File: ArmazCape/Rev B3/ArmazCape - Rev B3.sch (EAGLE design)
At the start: 166 parts, among them M1 7490100111A, Q1 32.768kHz, 12.5pF, Q2 ASE, Q4 IRLML6344TRPBF, Q5 IRLML6344TRPBF, U1 L7985A, U2 L7985A, U3 DS1307ZN+, U4 24AA256-I/SN, U5 CD4050BD, U6 CD4050BD, U7 PCA9685PW, U8 SN65HVD08D, U9 KSZ8851SNLI

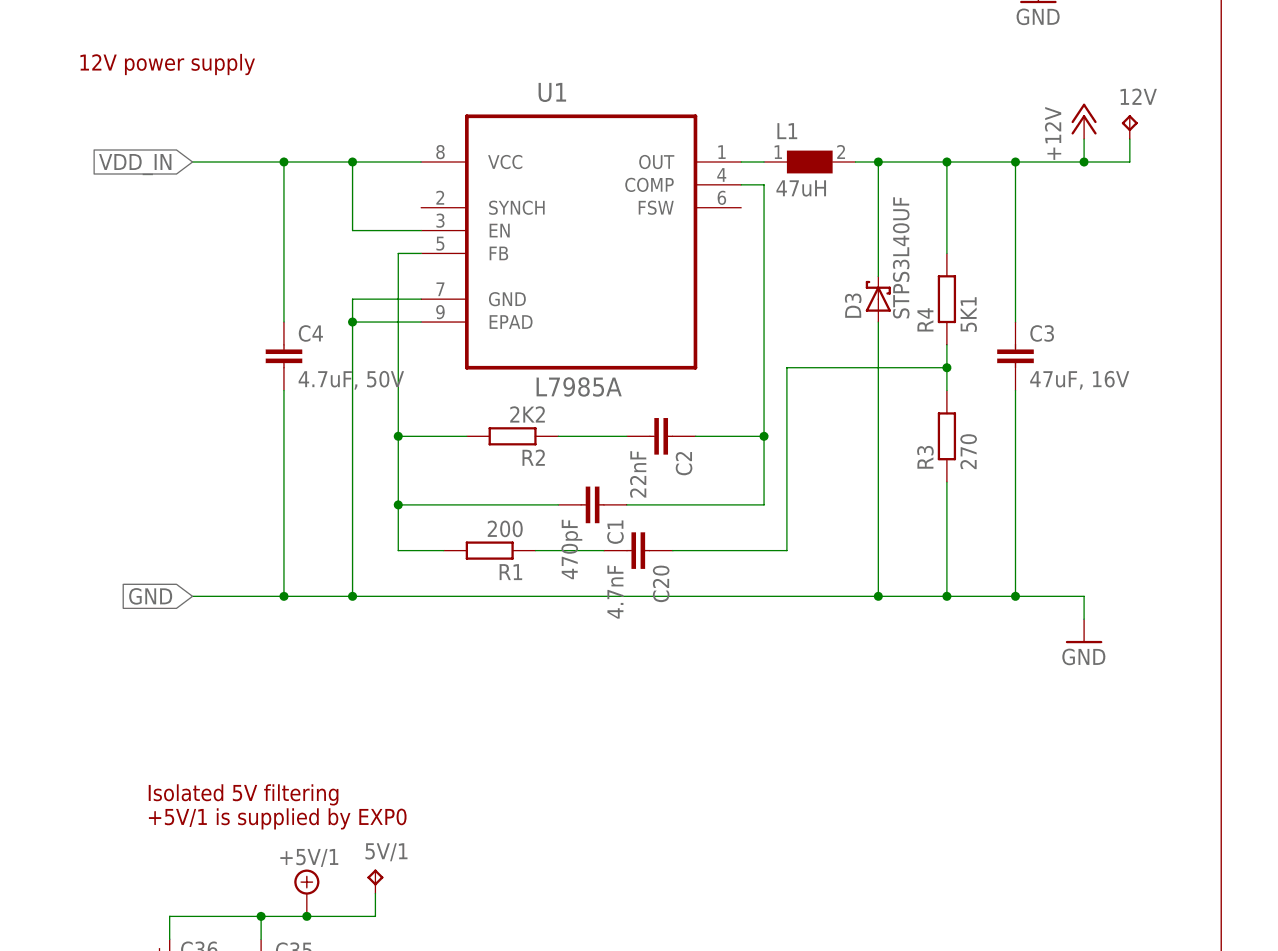
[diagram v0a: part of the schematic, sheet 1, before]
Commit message: Update L7985A FB on ArmazCape - RevB3. sch
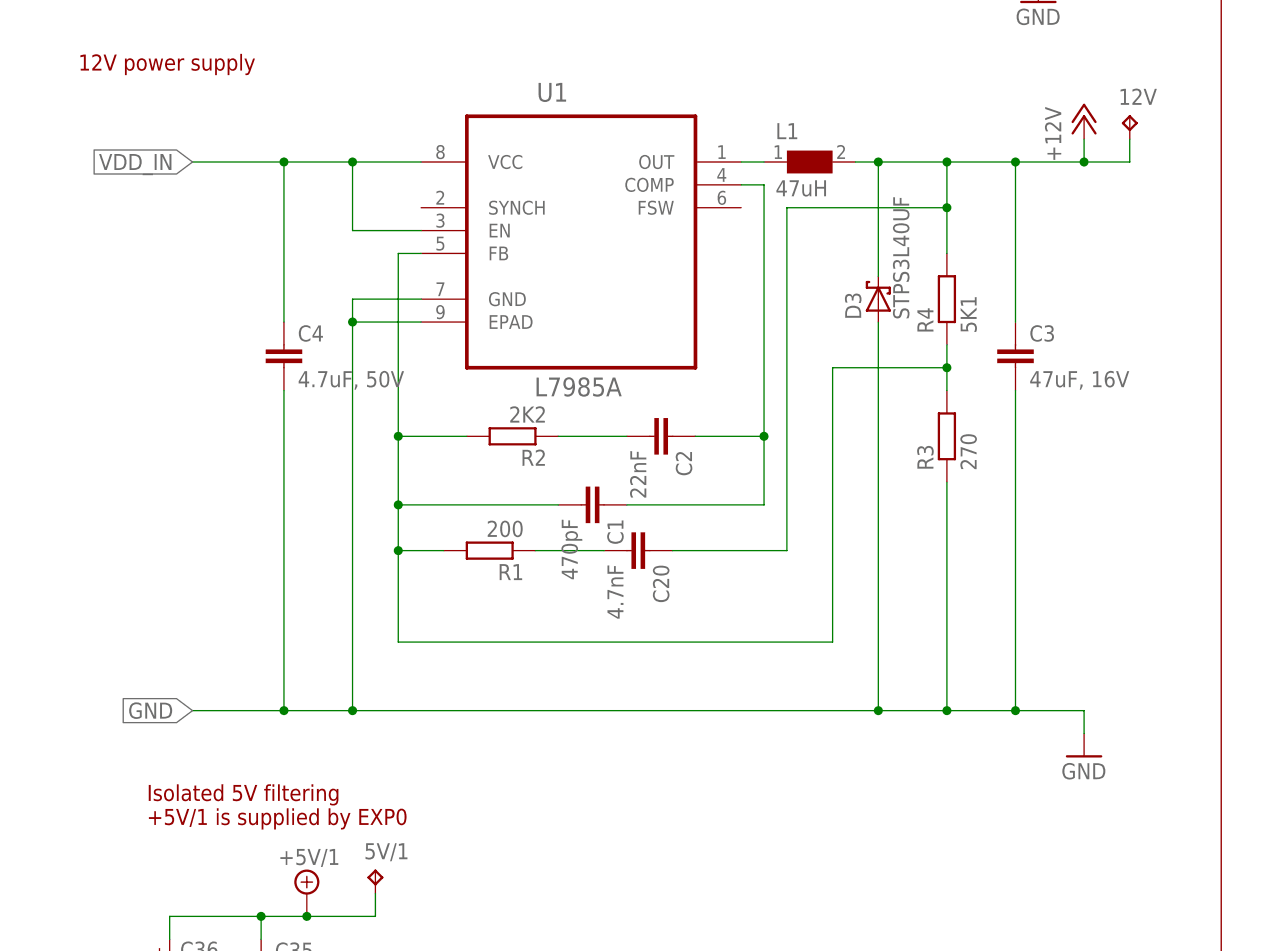
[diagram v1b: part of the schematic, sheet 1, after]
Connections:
- removed net N$36: C20.1, R3.2, R4.1
- removed net N$5: C1.2, R1.2, R2.2, U1.FB
- new net N$1: C1.2, R1.2, R2.2, R3.2, R4.1, U1.FB
- net +12V: now also C20.1
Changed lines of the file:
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@@
 <attribute name="MF" x="63.5" y="111.76" size="1.778" layer="96" display="off"/>
 </instance>
-<instance part="GND1" gate="1" x="119.38" y="63.5"/>
+<instance part="GND1" gate="1" x="119.38" y="50.8"/>
 <instance part="R2" gate="G$1" x="55.88" y="86.36" rot="R180">
 <attribute name="OC_FARNELL" x="55.88" y="86.36" size="1.778" layer="96" display="off"/>
@@
 <wire x1="45.72" y1="99.06" x2="38.1" y2="99.06" width="0.1524" layer="91"/>
 <pinref part="C4" gate="G$1" pin="2"/>
-<wire x1="30.48" y1="91.44" x2="30.48" y2="68.58" width="0.1524" layer="91"/>
-<wire x1="20.32" y1="68.58" x2="30.48" y2="68.58" width="0.1524" layer="91"/>
-<wire x1="30.48" y1="68.58" x2="38.1" y2="68.58" width="0.1524" layer="91"/>
-<junction x="30.48" y="68.58"/>
+<wire x1="30.48" y1="91.44" x2="30.48" y2="55.88" width="0.1524" layer="91"/>
+<wire x1="20.32" y1="55.88" x2="30.48" y2="55.88" width="0.1524" layer="91"/>
+<wire x1="30.48" y1="55.88" x2="38.1" y2="55.88" width="0.1524" layer="91"/>
+<junction x="30.48" y="55.88"/>
 <pinref part="C3" gate="G$1" pin="2"/>
-<wire x1="38.1" y1="68.58" x2="96.52" y2="68.58" width="0.1524" layer="91"/>
-<wire x1="96.52" y1="68.58" x2="104.14" y2="68.58" width="0.1524" layer="91"/>
-<wire x1="104.14" y1="68.58" x2="111.76" y2="68.58" width="0.1524" layer="91"/>
-<wire x1="111.76" y1="68.58" x2="111.76" y2="91.44" width="0.1524" layer="91"/>
+<wire x1="38.1" y1="55.88" x2="96.52" y2="55.88" width="0.1524" layer="91"/>
+<wire x1="96.52" y1="55.88" x2="104.14" y2="55.88" width="0.1524" layer="91"/>
+<wire x1="104.14" y1="55.88" x2="111.76" y2="55.88" width="0.1524" layer="91"/>
+<wire x1="111.76" y1="55.88" x2="111.76" y2="91.44" width="0.1524" layer="91"/>
 <pinref part="R3" gate="G$1" pin="1"/>
-<wire x1="104.14" y1="81.28" x2="104.14" y2="68.58" width="0.1524" layer="91"/>
-<junction x="104.14" y="68.58"/>
-<wire x1="96.52" y1="68.58" x2="96.52" y2="99.06" width="0.1524" layer="91"/>
-<junction x="96.52" y="68.58"/>
-<wire x1="38.1" y1="99.06" x2="38.1" y2="68.58" width="0.1524" layer="91"/>
+<wire x1="104.14" y1="81.28" x2="104.14" y2="55.88" width="0.1524" layer="91"/>
+<junction x="104.14" y="55.88"/>
+<wire x1="96.52" y1="55.88" x2="96.52" y2="99.06" width="0.1524" layer="91"/>
+<junction x="96.52" y="55.88"/>
+<wire x1="38.1" y1="99.06" x2="38.1" y2="55.88" width="0.1524" layer="91"/>
 <junction x="38.1" y="99.06"/>
-<junction x="38.1" y="68.58"/>
-<label x="20.32" y="68.58" size="1.778" layer="95" rot="R180" xref="yes"/>
-<wire x1="111.76" y1="68.58" x2="119.38" y2="68.58" width="0.1524" layer="91"/>
+<junction x="38.1" y="55.88"/>
+<label x="20.32" y="55.88" size="1.778" layer="95" rot="R180" xref="yes"/>
+<wire x1="111.76" y1="55.88" x2="119.38" y2="55.88" width="0.1524" layer="91"/>
 <pinref part="GND1" gate="1" pin="GND"/>
-<wire x1="119.38" y1="68.58" x2="119.38" y2="66.04" width="0.1524" layer="91"/>
+<wire x1="119.38" y1="55.88" x2="119.38" y2="53.34" width="0.1524" layer="91"/>
 <pinref part="D3" gate="A" pin="A"/>
-<junction x="111.76" y="68.58"/>
+<junction x="111.76" y="55.88"/>
 </segment>
 <segment>
@@
 </segment>
 </net>
-<net name="N$5" class="0">
-<segment>
-<pinref part="C1" gate="G$1" pin="2"/>
-<wire x1="60.96" y1="78.74" x2="43.18" y2="78.74" width="0.1524" layer="91"/>
-<pinref part="R2" gate="G$1" pin="2"/>
-<wire x1="50.8" y1="86.36" x2="43.18" y2="86.36" width="0.1524" layer="91"/>
-<wire x1="43.18" y1="86.36" x2="43.18" y2="106.68" width="0.1524" layer="91"/>
-<pinref part="U1" gate="A" pin="FB"/>
-<wire x1="43.18" y1="106.68" x2="45.72" y2="106.68" width="0.1524" layer="91"/>
-<wire x1="43.18" y1="73.66" x2="43.18" y2="78.74" width="0.1524" layer="91"/>
-<junction x="43.18" y="86.36"/>
-<wire x1="43.18" y1="78.74" x2="43.18" y2="86.36" width="0.1524" layer="91"/>
-<junction x="43.18" y="78.74"/>
-<pinref part="R1" gate="G$1" pin="2"/>
-<wire x1="48.26" y1="73.66" x2="43.18" y2="73.66" width="0.1524" layer="91"/>
-</segment>
-</net>
 <net name="N$6" class="1">
 <segment>
@@
 <junction x="111.76" y="116.84"/>
 <pinref part="R4" gate="G$1" pin="2"/>
-<wire x1="104.14" y1="116.84" x2="104.14" y2="106.68" width="0.1524" layer="91"/>
+<wire x1="104.14" y1="116.84" x2="104.14" y2="111.76" width="0.1524" layer="91"/>
 <junction x="104.14" y="116.84"/>
 <pinref part="P+1" gate="1" pin="+12V"/>
 <pinref part="D3" gate="A" pin="C"/>
+<wire x1="104.14" y1="111.76" x2="104.14" y2="106.68" width="0.1524" layer="91"/>
 <wire x1="96.52" y1="104.14" x2="96.52" y2="116.84" width="0.1524" layer="91"/>
 <junction x="96.52" y="116.84"/>
@@
 <wire x1="124.46" y1="116.84" x2="124.46" y2="119.38" width="0.1524" layer="91"/>
 <junction x="119.38" y="116.84"/>
+<wire x1="86.36" y1="111.76" x2="86.36" y2="73.66" width="0.1524" layer="91"/>
+<wire x1="86.36" y1="73.66" x2="73.66" y2="73.66" width="0.1524" layer="91"/>
+<pinref part="C20" gate="G$1" pin="1"/>
+<wire x1="86.36" y1="111.76" x2="104.14" y2="111.76" width="0.1524" layer="91"/>
+<junction x="104.14" y="111.76"/>
 </segment>
 </net>
@@
 <pinref part="C20" gate="G$1" pin="2"/>
 <wire x1="66.04" y1="73.66" x2="58.42" y2="73.66" width="0.1524" layer="91"/>
-</segment>
-</net>
-<net name="N$36" class="0">
-<segment>
-<pinref part="R3" gate="G$1" pin="2"/>
-<pinref part="R4" gate="G$1" pin="1"/>
-<wire x1="104.14" y1="96.52" x2="104.14" y2="93.98" width="0.1524" layer="91"/>
-<wire x1="104.14" y1="93.98" x2="104.14" y2="91.44" width="0.1524" layer="91"/>
-<junction x="104.14" y="93.98"/>
-<wire x1="104.14" y1="93.98" x2="86.36" y2="93.98" width="0.1524" layer="91"/>
-<wire x1="86.36" y1="93.98" x2="86.36" y2="73.66" width="0.1524" layer="91"/>
-<wire x1="86.36" y1="73.66" x2="73.66" y2="73.66" width="0.1524" layer="91"/>
-<pinref part="C20" gate="G$1" pin="1"/>
 </segment>
 </net>
@@
 </segment>
 </net>
+<net name="N$1" class="0">
+<segment>
+<pinref part="C1" gate="G$1" pin="2"/>
+<wire x1="60.96" y1="78.74" x2="43.18" y2="78.74" width="0.1524" layer="91"/>
+<pinref part="R2" gate="G$1" pin="2"/>
+<wire x1="50.8" y1="86.36" x2="43.18" y2="86.36" width="0.1524" layer="91"/>
+<wire x1="43.18" y1="86.36" x2="43.18" y2="106.68" width="0.1524" layer="91"/>
+<pinref part="U1" gate="A" pin="FB"/>
+<wire x1="43.18" y1="106.68" x2="45.72" y2="106.68" width="0.1524" layer="91"/>
+<wire x1="43.18" y1="73.66" x2="43.18" y2="78.74" width="0.1524" layer="91"/>
+<junction x="43.18" y="86.36"/>
+<wire x1="43.18" y1="78.74" x2="43.18" y2="86.36" width="0.1524" layer="91"/>
+<junction x="43.18" y="78.74"/>
+<pinref part="R1" gate="G$1" pin="2"/>
+<wire x1="48.26" y1="73.66" x2="43.18" y2="73.66" width="0.1524" layer="91"/>
+<wire x1="43.18" y1="73.66" x2="43.18" y2="63.5" width="0.1524" layer="91"/>
+<wire x1="43.18" y1="63.5" x2="91.44" y2="63.5" width="0.1524" layer="91"/>
+<junction x="43.18" y="73.66"/>
+<wire x1="91.44" y1="63.5" x2="91.44" y2="93.98" width="0.1524" layer="91"/>
+<pinref part="R3" gate="G$1" pin="2"/>
+<pinref part="R4" gate="G$1" pin="1"/>
+<wire x1="104.14" y1="96.52" x2="104.14" y2="93.98" width="0.1524" layer="91"/>
+<wire x1="104.14" y1="93.98" x2="104.14" y2="91.44" width="0.1524" layer="91"/>
+<wire x1="91.44" y1="93.98" x2="104.14" y2="93.98" width="0.1524" layer="91"/>
+<junction x="104.14" y="93.98"/>
+</segment>
+</net>

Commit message: Added GERBER RS274X files for Varmo - Rev A1
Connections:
- removed net N$31: OK2.C, R36.2
- removed net N$6: L1.1, U1.OUT
- new net N$30: D3.C, L1.1, U1.OUT
- new net N$5: OK2.A, R36.2
- net +12V: no longer D3.C
- net +5V: no longer D4.C
- net +5V/1: no longer OK2.A
- net GND1: now also OK2.C
- net N$19: now also D4.C
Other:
- moved on the sheet: D3, D4, L1, L4, R36

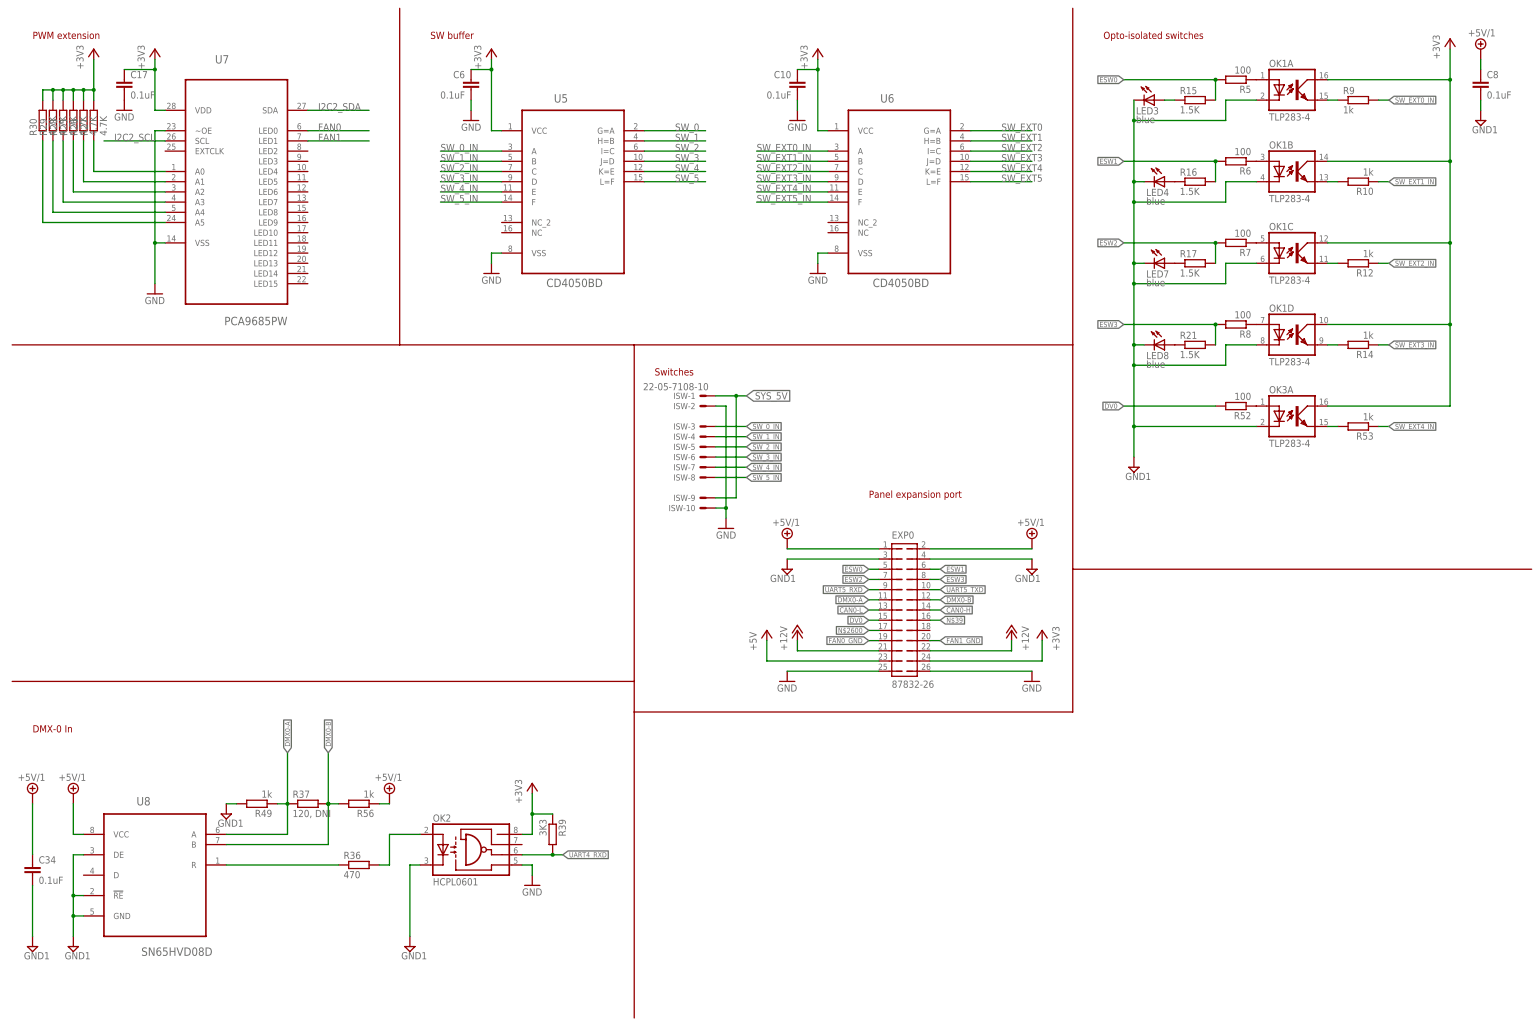
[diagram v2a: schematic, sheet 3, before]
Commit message: ArmazCape - Rev B3 updated:
Fix for +5V and +12V power chips
Routed KSZ8851SNL according to Evaluation-board schematics
Modified 7490100111A symbol to avoid future mistakes
Moved KSZ8851SNL RSTN to P9.12 instead of SYS_RESET
Moved SW_0 to P9.14 (pin conflict)
Added pulldown on all buffer inputs
TLP283 output +5V to trigger input buffer
Added pulldown on SN65HVD08D on R pin

Reduced fuse holder spacing
Reduced width on keystone 3000 footprint
Moved CC-BY-SA to tPlace layer
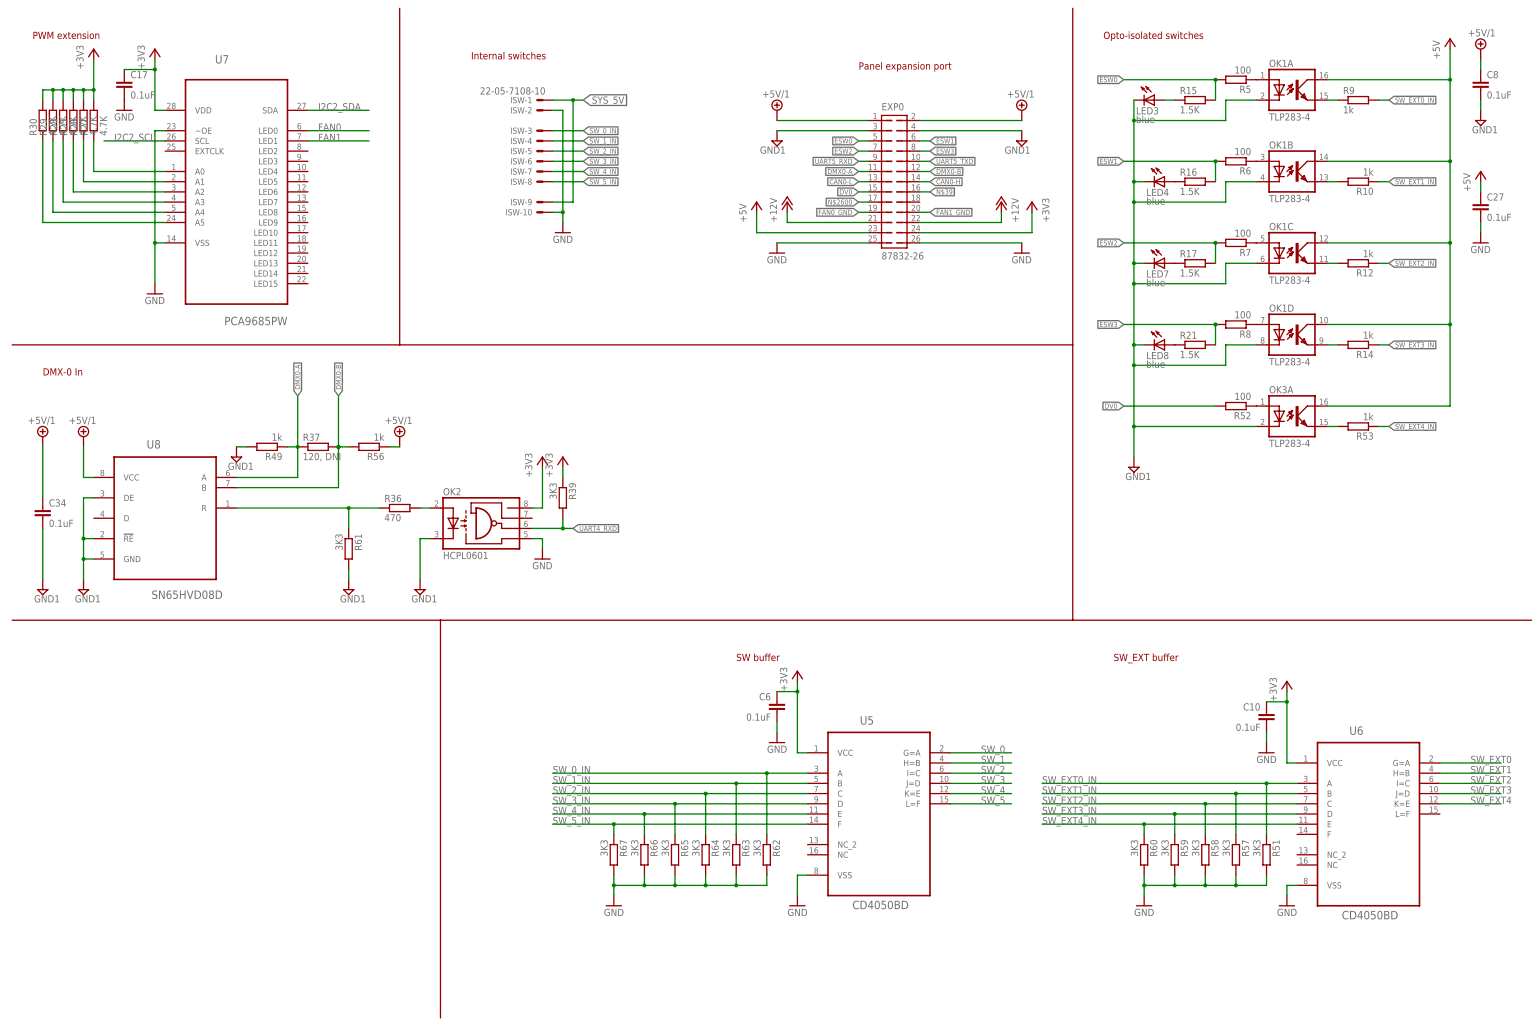
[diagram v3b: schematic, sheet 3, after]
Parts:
- added C37: 1000pF, 2kV, rcl:C-EUC1206
- added R57, R58, R59, R60, R61, R62, R63, R64, R65, R66, R67: 3K3, rcl:R-EU_R0603
- C18: device rcl:C-EUC1210 -> rcl:C-EUC1206
- C27: value 0.01uF -> 0.1uF; MPN MC0603B103K160CT -> MC0603B104K250CT; OC_FARNELL 1759003 -> 1759037
- C29: value 6.8nF -> 0.01uF; MPN MC0603B682K500CT -> MC0603B103K160CT; OC_FARNELL 1759100 -> 1759003
- C30: value 6.8nF -> 4.7uF; device rcl:C-EUC0603 -> rcl:CPOL-EUCT3216; MF MULTICOMP -> AVX (FORMERLY KNOWN AS NICHICON); MPN MC0603B682K500CT -> F931A475MAA; OC_FARNELL 1759100 -> 1818579
- ISW: OC_FARNELL 9731660 -> (none)
- R11: device rcl:R-EU_R0603 -> rcl:R-EU_R0402
- R23, R42, R43, R44: MPN MCMR06X7501FTL -> MCMR06X750 JTL; OC_FARNELL 2073570 -> 2073569
- R3: MPN MCMR06X2000FTL -> MCMR06X2700FTL; OC_FARNELL 2073417 -> 2073451
- R39: MPN MCMR04X3301FTL -> MC0063W060313K3; OC_FARNELL 2072928 -> 9331026
- R51: value 10 -> 3K3; MPN MCMR04X6980FTL -> MC0063W060313K3; OC_FARNELL 2073217 -> 9331026
- R55: MPN MCMR06X4701FTL -> MCMR06X3011FTL; OC_FARNELL 2073509 -> 2073464
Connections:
- net SPI1_INT renamed !KSZ8851_INT
- removed net N$2000: C29.1, R48.2, U9.RXP
- removed net N$300: C30.1, R50.2, U9.RXM
- removed net N$4200: M1.TDI+, R45.2, U9.TXP
- removed net N$4400: M1.TDI-, R46.1, U9.TXM
- removed net N$50: C25.1, M1.RXCTI, R48.1, R50.1
- removed net N$51: C29.2, M1.RDI+
- removed net SW_EXT5: U6.L=F
- removed net SW_EXT5_IN: U6.F
- new net !KSZ8851_RST: BB1P9.12, U9.!RST
- new net GNDI: C18.2, C37.2, ETH0.M1, ETH0.M2
- new net N$31: M1.RDIM, R45.2, U9.RXM
- new net N$36: M1.TDIP, R50.1, U9.TXP
- new net N$37: M1.TDIM, R48.1, U9.TXM
- new net N$6: ETH0.6, M1.TDOM
- net +3V3: now also C30.+, M1.RXCTI, M1.TXCTI; no longer OK1A.COL, OK1B.COL, OK1C.COL, OK1D.COL, OK3A.COL, R45.1, R46.2, R51.1
- net +5V: now also C27.1, OK1A.COL, OK1B.COL, OK1C.COL, OK1D.COL, OK3A.COL
- net GND: now also C29.2, C30.-, C37.1, R51.2, R57.2, R58.2, R59.2, R60.2, R62.2, R63.2, R64.2, R65.2, R66.2, R67.2; no longer C18.2
- net GND1: now also R61.2
- net N$27: now also R61.1
- net N$4: now also M1.RDIP, R46.2, U9.RXP; no longer C30.2, M1.RDI-
- net N$40: now also M1.RXOP; no longer M1.TDO+
- net N$41: now also M1.RDOM; no longer M1.TDO-
- net N$42: now also M1.TDOP; no longer M1.RDO+
- net N$43: now also C25.1, R48.2, R50.2; no longer ETH0.6, M1.RXO-
- net N$49: now also C29.1, R45.1, R46.1; no longer C27.1, M1.TXCTI, R51.2
- net SW_0: now also BB1P9.14; no longer BB1P9.25
- net SW_0_IN: now also R62.1
- net SW_1_IN: now also R63.1
- net SW_2_IN: now also R64.1
- net SW_3_IN: now also R65.1
- net SW_4_IN: now also R66.1
- net SW_5_IN: now also R67.1
- net SW_EXT0_IN: now also R51.1
- net SW_EXT1_IN: now also R57.1
- net SW_EXT2_IN: now also R58.1
- net SW_EXT3_IN: now also R59.1
- net SW_EXT4_IN: now also R60.1
- net SYS_RESET: no longer U9.!RST
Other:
- note added: "Internal switches"
- note added: "SW_EXT buffer"
- note removed: "Switches"
- moved on the sheet: B1, C10, C13, C15, C16, C18, C21, C22, C24, C25, C29, C31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
